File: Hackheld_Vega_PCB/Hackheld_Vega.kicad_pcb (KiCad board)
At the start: 2 copper layers, 50.5 x 67.1 mm, 35 parts, among them J1 Conn_01x04_Female, J2 Conn_01x03_Female, SW1 SW_Push, SW2 SW_Push, SW3 SW_Push, SW4 SW_Push, SW5 SW_Push, SW6 SW_Push, U1 D1_mini

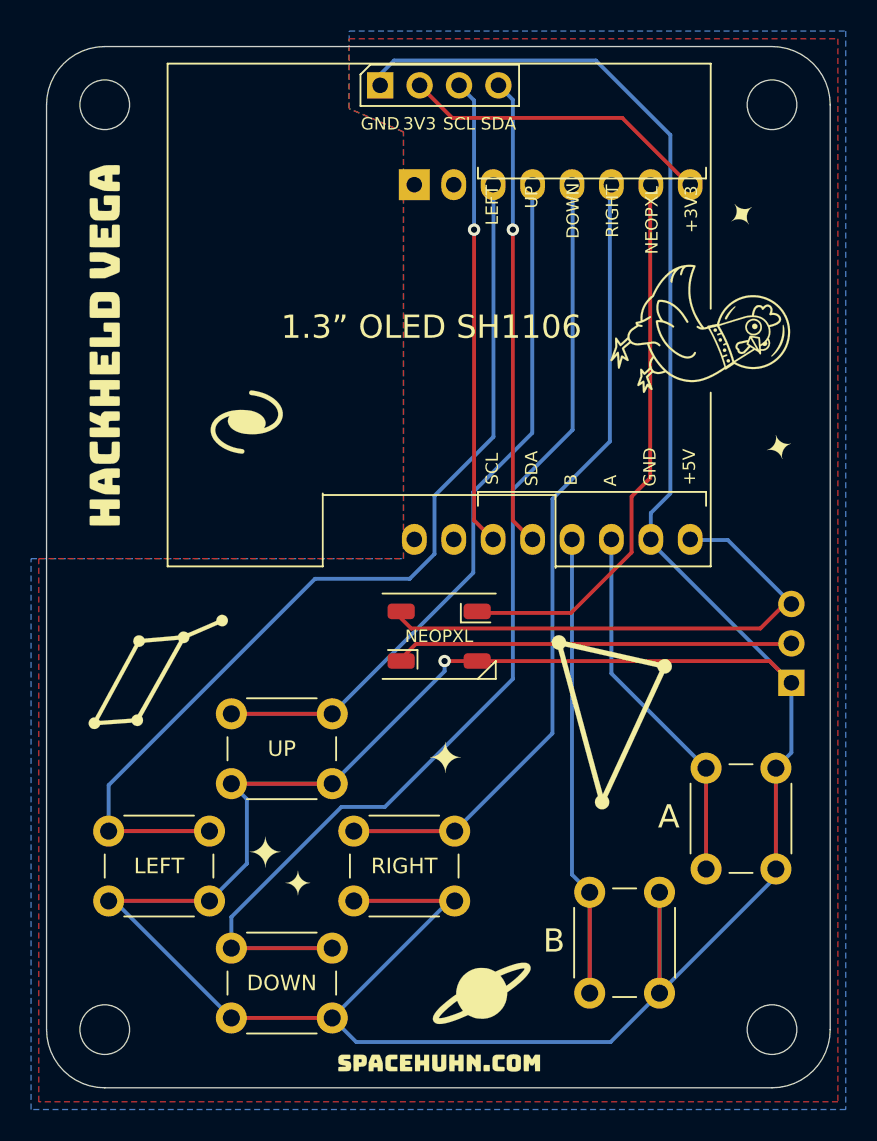
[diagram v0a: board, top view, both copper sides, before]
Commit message: removed redundant traces, removed <90deg trace angles, connected GND pours, alignment/centering of traces
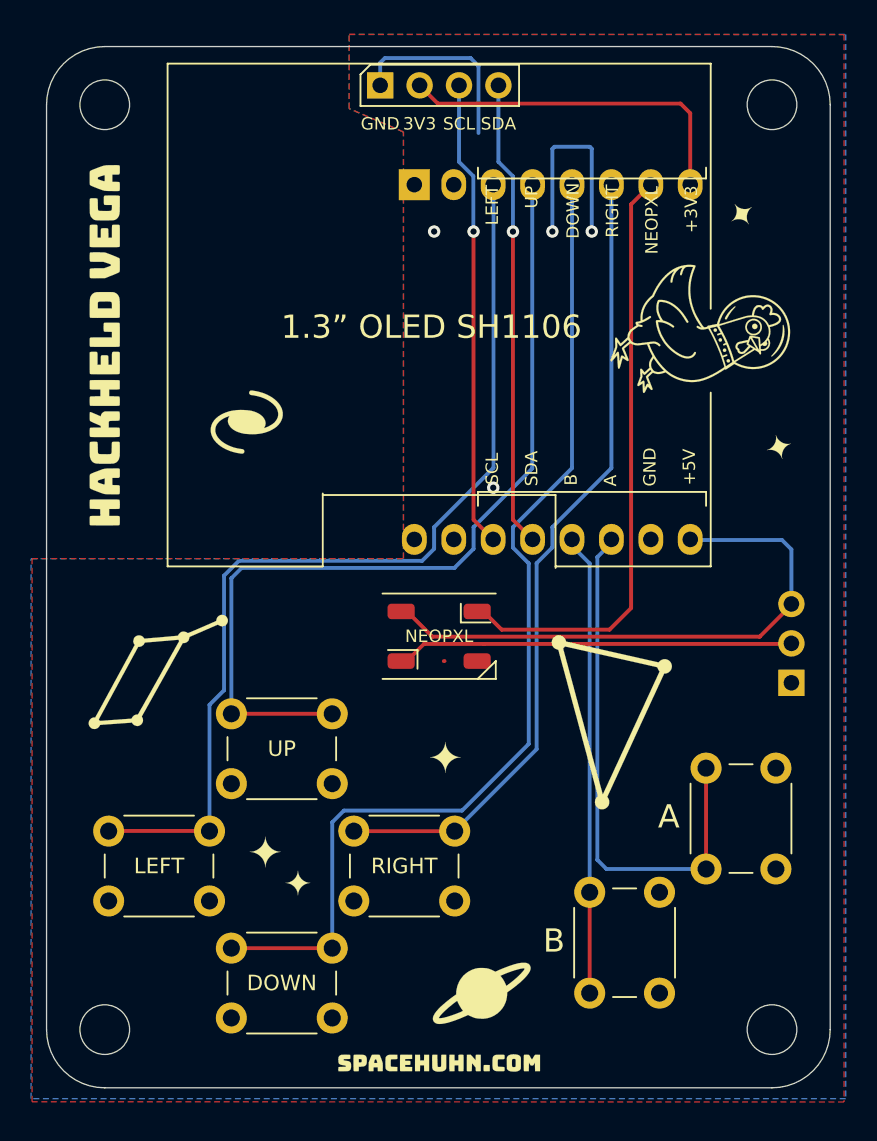
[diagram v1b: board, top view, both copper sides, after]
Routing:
- net GND: track 244.5 -> 28.9 mm, vias 1 -> 4
- net /B: track 36.2 -> 29.7 mm
- net /RIGHT: track 58.8 -> 52.3 mm
- net /LEFT: track 68.6 -> 62.7 mm
- net /DOWN: track 73.7 -> 68.1 mm
- net /A: track 30.3 -> 34.8 mm
- net /UP: track 52.5 -> 56.7 mm
- net /NEOPIXEL: track 36.3 -> 39.3 mm
- net +3V3: track 20.0 -> 22.8 mm
- net +5V: track 36.1 -> 38.6 mm
- added copper zone on B.Cu, net GND
- added copper zone on F.Cu, net GND
- removed copper zone on B.Cu, net (none)
- removed copper zone on F.Cu, net (none)
